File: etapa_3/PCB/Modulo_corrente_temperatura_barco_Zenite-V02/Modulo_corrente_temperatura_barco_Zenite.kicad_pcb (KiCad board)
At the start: 2 copper layers, 60 x 138.6 mm, 47 parts, among them J1 RJ45_Shielded, J2 RJ45_Shielded, J3 Conn_01x03, U2 LM7805, U3 TLV2376IDGKR, U4 MCP2515-xSO, U5 MCP2551-I-SN, Y1 16MHz

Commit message: minor ajustmentes in PCB laytout and schem
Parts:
- J3: value Conn_01x03 -> 2edgrc; footprint pi-III-lib:B3BXHALFSN -> pi-III-lib:2EDRC_4pins
- R14, R8: footprint Resistor_SMD:R_2010_5025Metric_Pad1.40x2.65mm_HandSolder -> Resistor_SMD:R_1206_3216Metric_Pad1.30x1.75mm_HandSolder
- moved J3 12.8 mm to (116.7, 46.2), turned to -90 degrees
- moved R14 1.63 mm to (113.0, 77.2)
- moved R8 0.84 mm to (113.0, 74.6)
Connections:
- J3 pad 1: 12V -> neg12V
- J3 pad 2: I_signal -> 12V
- J3 pad 3: neg12V -> I_signal
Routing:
- net neg12V: track 20.2 -> 13.9 mm
- net AGND: track 3.38 -> 0.00 mm, vias 0 -> 2
- net 12V: track 30.8 -> 33.9 mm
- net I_signal: track 53.8 -> 51.6 mm

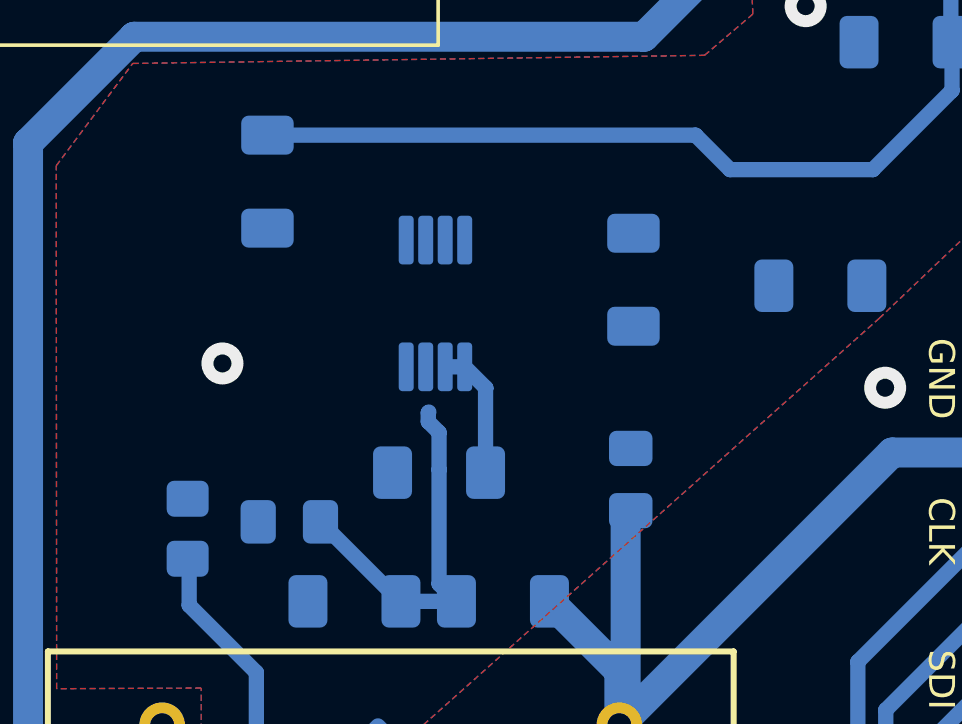
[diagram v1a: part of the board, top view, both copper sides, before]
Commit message: Roteamento do AmpOP
Roteamento do AMpOP na v2.0 da placa - ainda verificando melhorias
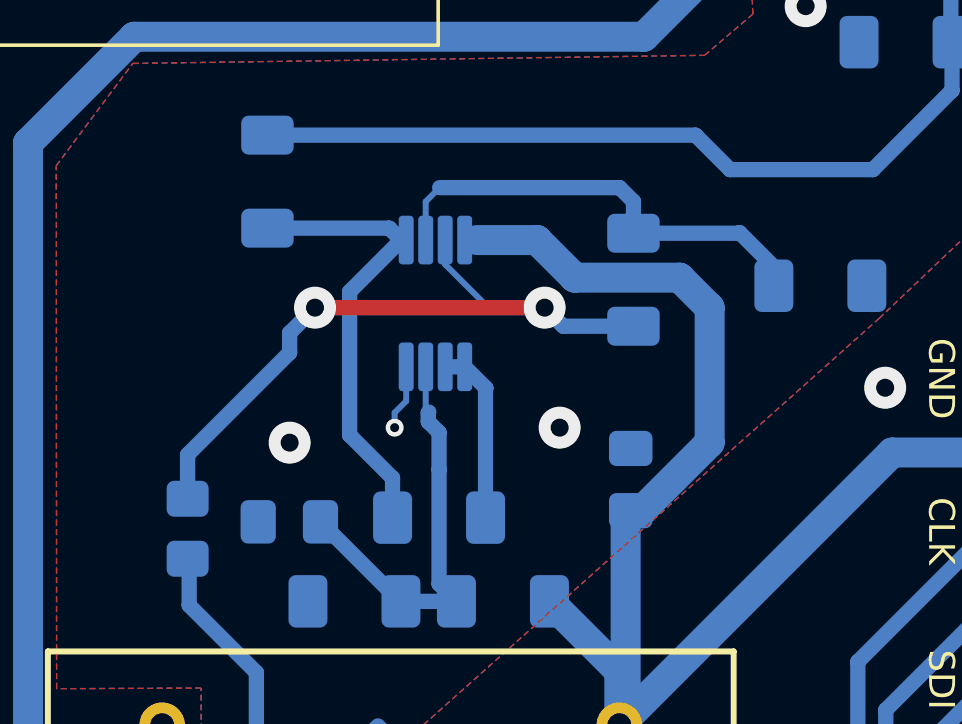
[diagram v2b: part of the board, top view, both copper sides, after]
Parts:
- moved R6 1.50 mm to (97.5, 93.0)
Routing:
- net Net-(R9-Pad1): track 0.00 -> 23.7 mm, vias 0 -> 2
- net 3V3: track 139.0 -> 155.5 mm
- net Net-(U3B--): track 0.00 -> 15.4 mm
- net Net-(U3B-+): track 0.00 -> 15.2 mm
- net AGND: track 0.00 -> 2.19 mm, vias 2 -> 4
- net Net-(U3A-+): track 12.3 -> 13.9 mm
- net Net-(U3A--): track 4.42 -> 5.92 mm

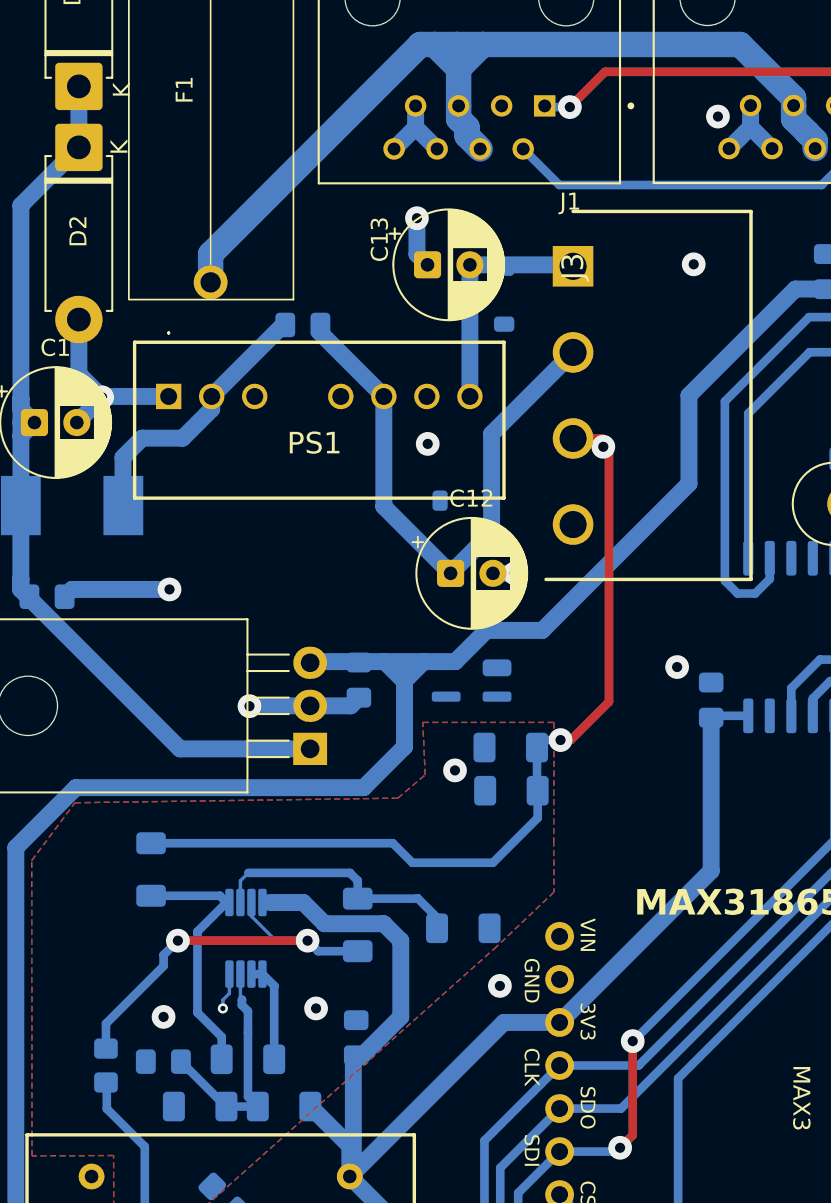
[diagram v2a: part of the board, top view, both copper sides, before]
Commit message: ampop traces modified
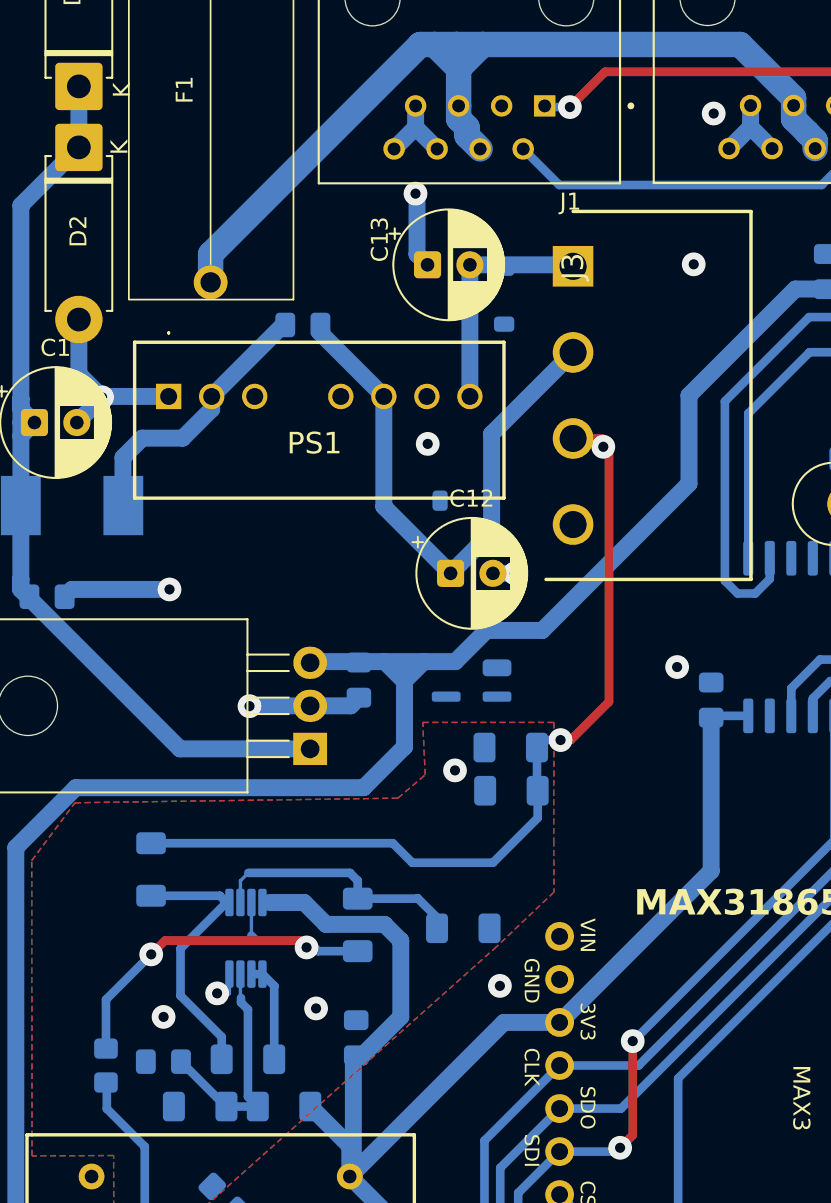
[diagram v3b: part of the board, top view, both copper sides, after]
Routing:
- net GND: track 52.8 -> 54.3 mm
- net Net-(R9-Pad1): track 23.7 -> 25.0 mm
- net Net-(U3B-+): track 15.2 -> 16.0 mm
- net AGND: track 2.19 -> 2.79 mm
